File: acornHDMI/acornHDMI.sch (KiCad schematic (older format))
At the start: 33 parts, among them J1 0.1\" grid male, J2 8P8C_Shielded, J3 HDMI_A, U1 PTN3381D, U2 PCA9534

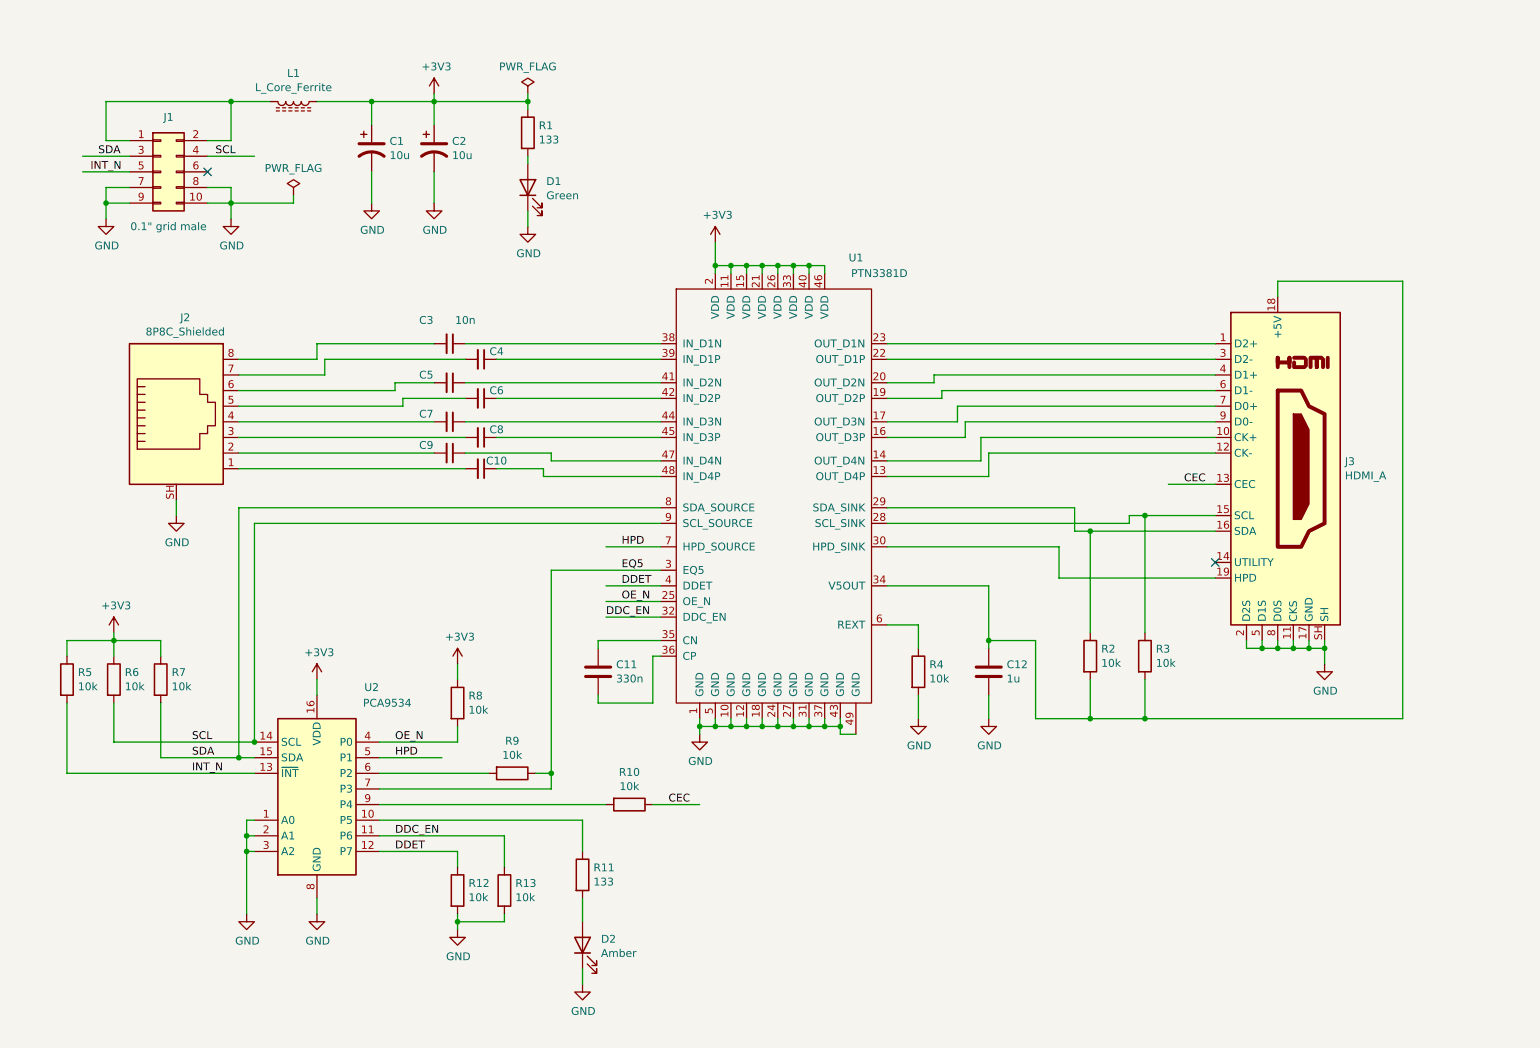
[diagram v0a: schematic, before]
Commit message: change PTN3381D to B
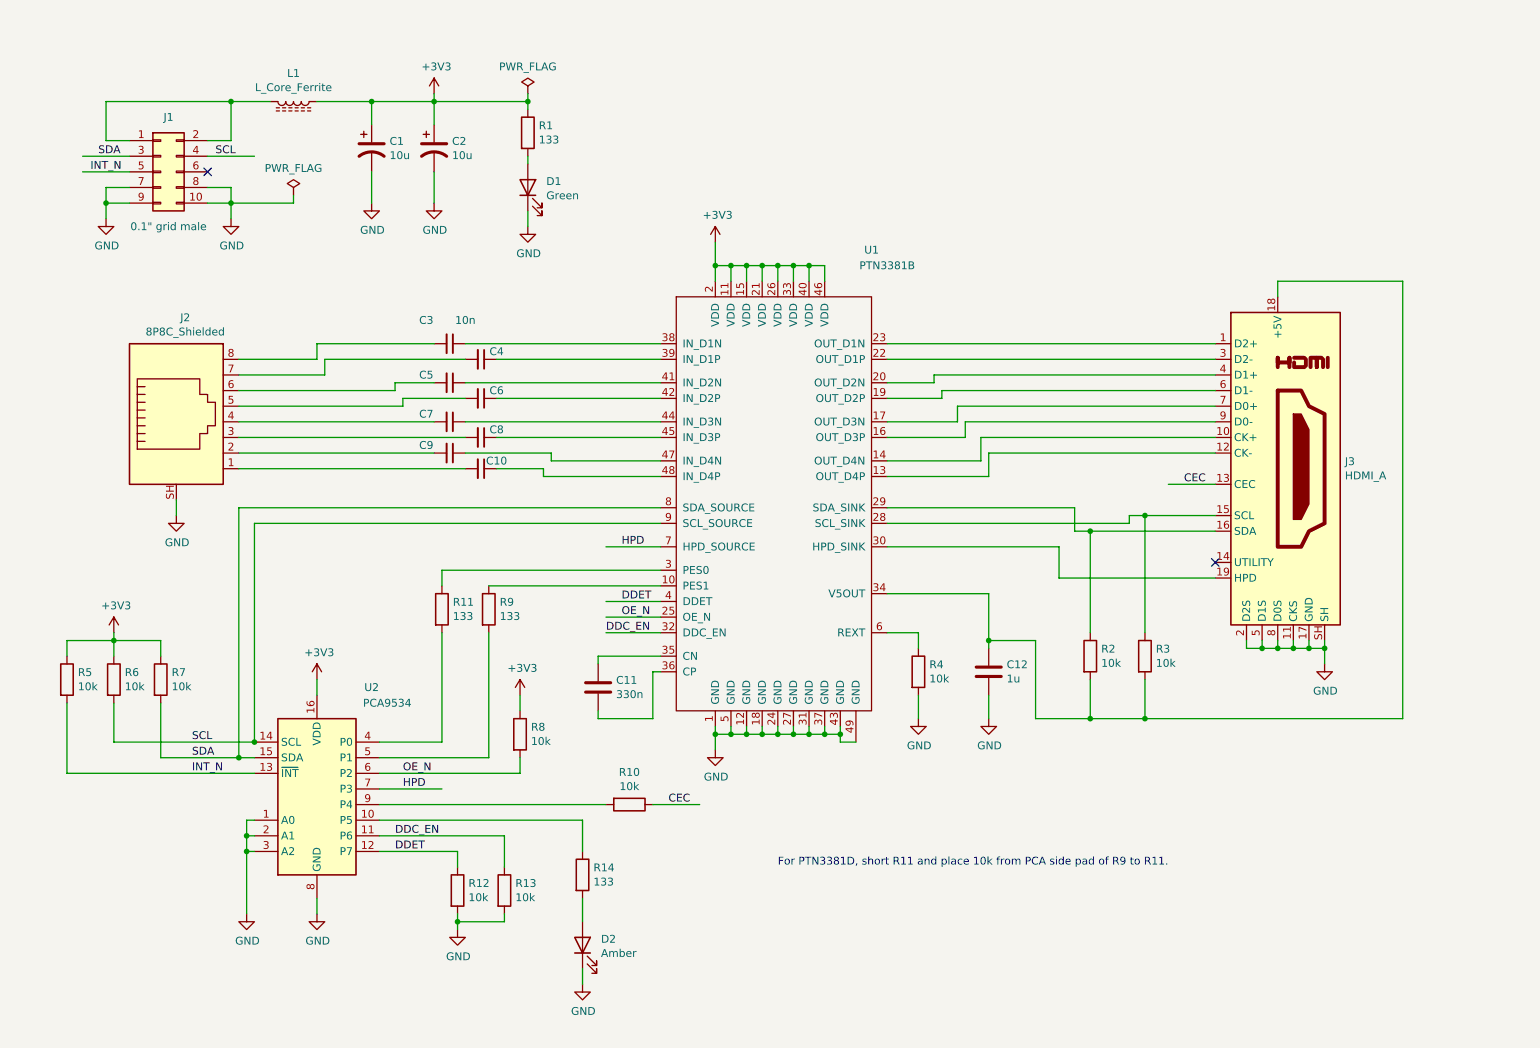
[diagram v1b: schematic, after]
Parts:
- removed U1: PTN3381D, Package_DFN_QFN:QFN-48-1EP_7x7mm_P0.5mm_EP5.15x5.15mm, symbol local:PTN3381D
- added R14: 133, Resistor_SMD:R_0603_1608Metric_Pad0.98x0.95mm_HandSolder, symbol Device:R
- added U1: PTN3381B, Package_DFN_QFN:QFN-48-1EP_7x7mm_P0.5mm_EP5.15x5.15mm, symbol local:PTN3381B
- R9: value 10k -> 133
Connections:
- net labels removed: EQ5
- wire segments 220 -> 219
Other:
- note added: "For PTN3381D, short R11 and place 10k from PCA side pad of R9 to R11."
- moved on the sheet: C11, R11, R8
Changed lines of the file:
@@
 $EndDescr
-$Comp
-L local:PTN3381D U1
-U 1 1 60D4AADB
-P 5400 5200
-F 0 "U1" H 5950 8050 50  0000 C CNN
-F 1 "PTN3381D" H 6100 7950 50  0000 C CNN
-F 2 "Package_DFN_QFN:QFN-48-1EP_7x7mm_P0.5mm_EP5.15x5.15mm" H 5400 5250 50  0001 C CNN
-F 3 "" H 5400 5250 50  0001 C CNN
-	1    5400 5200
-	1    0    0    -1
-$EndComp
 $Comp
 L Connector:HDMI_A J3
@@
 $EndComp
 Wire Wire Line
-	6150 4700 6350 4700
-Wire Wire Line
 	6350 5150 6350 5300
 $Comp
@@
 L power:GND #PWR0102
 U 1 1 60D5A843
-P 4950 5400
-F 0 "#PWR0102" H 4950 5150 50  0001 C CNN
-F 1 "GND" H 4955 5227 50  0000 C CNN
-F 2 "" H 4950 5400 50  0001 C CNN
-F 3 "" H 4950 5400 50  0001 C CNN
-	1    4950 5400
-	1    0    0    -1
-$EndComp
-Wire Wire Line
-	4950 5400 4950 5350
-Wire Wire Line
-	4950 5350 5050 5350
-Wire Wire Line
-	5050 5350 5050 5300
-Connection ~ 4950 5350
-Wire Wire Line
-	4950 5350 4950 5300
-Wire Wire Line
-	5150 5300 5150 5350
-Wire Wire Line
-	5150 5350 5050 5350
-Connection ~ 5050 5350
-Wire Wire Line
-	5250 5300 5250 5350
-Wire Wire Line
-	5250 5350 5150 5350
-Connection ~ 5150 5350
-Wire Wire Line
-	5350 5300 5350 5350
-Wire Wire Line
-	5350 5350 5250 5350
-Connection ~ 5250 5350
-Wire Wire Line
-	5950 5400 5850 5400
-Wire Wire Line
-	5850 5400 5850 5350
-Wire Wire Line
-	5850 5350 5750 5350
-Connection ~ 5350 5350
-Wire Wire Line
-	5850 5300 5850 5350
-Connection ~ 5850 5350
-Wire Wire Line
-	5750 5300 5750 5350
-Connection ~ 5750 5350
-Wire Wire Line
-	5750 5350 5650 5350
-Wire Wire Line
-	5650 5300 5650 5350
-Connection ~ 5650 5350
-Wire Wire Line
-	5650 5350 5550 5350
-Wire Wire Line
-	5550 5300 5550 5350
-Connection ~ 5550 5350
-Wire Wire Line
-	5550 5350 5450 5350
-Wire Wire Line
-	5450 5300 5450 5350
-Connection ~ 5450 5350
-Wire Wire Line
-	5450 5350 5350 5350
+P 5050 5500
+F 0 "#PWR0102" H 5050 5250 50  0001 C CNN
+F 1 "GND" H 5055 5327 50  0000 C CNN
+F 2 "" H 5050 5500 50  0001 C CNN
+F 3 "" H 5050 5500 50  0001 C CNN
+	1    5050 5500
+	1    0    0    -1
+$EndComp
+Wire Wire Line
+	5050 5400 5050 5350
+Wire Wire Line
+	5150 5350 5150 5400
+Wire Wire Line
+	5150 5400 5050 5400
+Wire Wire Line
+	5250 5350 5250 5400
+Wire Wire Line
+	5250 5400 5150 5400
+Connection ~ 5150 5400
+Wire Wire Line
+	5350 5350 5350 5400
+Wire Wire Line
+	5350 5400 5250 5400
+Connection ~ 5250 5400
+Wire Wire Line
+	5950 5450 5850 5450
+Wire Wire Line
+	5850 5450 5850 5400
+Wire Wire Line
+	5850 5400 5750 5400
+Connection ~ 5350 5400
+Wire Wire Line
+	5850 5350 5850 5400
+Connection ~ 5850 5400
+Wire Wire Line
+	5750 5350 5750 5400
+Connection ~ 5750 5400
+Wire Wire Line
+	5750 5400 5650 5400
+Wire Wire Line
+	5650 5350 5650 5400
+Connection ~ 5650 5400
+Wire Wire Line
+	5650 5400 5550 5400
+Wire Wire Line
+	5550 5350 5550 5400
+Connection ~ 5550 5400
+Wire Wire Line
+	5550 5400 5450 5400
+Wire Wire Line
+	5450 5350 5450 5400
+Connection ~ 5450 5400
+Wire Wire Line
+	5450 5400 5350 5400
 Wire Wire Line
 	6150 2900 8250 2900
@@
 	8850 4850 8950 4850
 Wire Wire Line
-	6150 4450 6800 4450
-Wire Wire Line
 	9450 5300 9450 2500
 Wire Wire Line
@@
 $EndComp
 Wire Wire Line
-	6350 4850 6350 4700
+	6350 4850 6350 4750
 Wire Wire Line
 	7250 4200 7250 4400
@@
 Connection ~ 6800 4800
 Wire Wire Line
-	6800 4800 6800 4450
+	6800 4800 6800 4500
 Wire Wire Line
 	7100 5300 7450 5300
@@
 L Device:C C11
 U 1 1 60DBDA44
-P 4300 5000
-F 0 "C11" H 4415 5046 50  0000 L CNN
-F 1 "330n" H 4415 4955 50  0000 L CNN
-F 2 "Capacitor_SMD:C_0603_1608Metric_Pad1.08x0.95mm_HandSolder" H 4338 4850 50  0001 C CNN
-F 3 "~" H 4300 5000 50  0001 C CNN
-	1    4300 5000
+P 4300 5100
+F 0 "C11" H 4415 5146 50  0000 L CNN
+F 1 "330n" H 4415 5055 50  0000 L CNN
+F 2 "Capacitor_SMD:C_0603_1608Metric_Pad1.08x0.95mm_HandSolder" H 4338 4950 50  0001 C CNN
+F 3 "~" H 4300 5100 50  0001 C CNN
+	1    4300 5100
 	1    0    0    -1
 $EndComp
@@
 	3650 3000 4700 3000
 Wire Wire Line
-	4700 4800 4300 4800
-Wire Wire Line
-	4300 4800 4300 4850
-Wire Wire Line
-	4300 5150 4300 5200
-Wire Wire Line
-	4300 5200 4650 5200
-Wire Wire Line
-	4650 5200 4650 4900
-Wire Wire Line
-	4650 4900 4700 4900
-Text Label 3000 5450 0    50   ~ 0
+	4700 4900 4300 4900
+Wire Wire Line
+	4300 4900 4300 4950
+Wire Wire Line
+	4300 5250 4300 5300
+Wire Wire Line
+	4300 5300 4650 5300
+Text Label 3050 5650 0    50   ~ 0
 OE_N
 Wire Wire Line
+	4350 4650 4700 4650
+Text Label 4450 4650 0    50   ~ 0
+OE_N
+Wire Wire Line
 	4350 4550 4700 4550
+Wire Wire Line
+	4350 4750 4700 4750
 Text Label 4450 4550 0    50   ~ 0
-OE_N
-Wire Wire Line
-	4350 4450 4700 4450
-Wire Wire Line
-	4350 4650 4700 4650
-Text Label 4450 4450 0    50   ~ 0
 DDET
 Text Label 3000 6150 0    50   ~ 0
@@
 L Device:R R8
 U 1 1 60E82787
-P 3400 5200
-F 0 "R8" H 3470 5246 50  0000 L CNN
-F 1 "10k" H 3470 5155 50  0000 L CNN
-F 2 "Resistor_SMD:R_0603_1608Metric_Pad0.98x0.95mm_HandSolder" V 3330 5200 50  0001 C CNN
-F 3 "~" H 3400 5200 50  0001 C CNN
-	1    3400 5200
-	1    0    0    -1
-$EndComp
-Wire Wire Line
-	3400 5450 3400 5350
-Wire Wire Line
-	2900 5450 3400 5450
-Text Label 4350 4650 0    50   ~ 0
+P 3800 5400
+F 0 "R8" H 3870 5446 50  0000 L CNN
+F 1 "10k" H 3870 5355 50  0000 L CNN
+F 2 "Resistor_SMD:R_0603_1608Metric_Pad0.98x0.95mm_HandSolder" V 3730 5400 50  0001 C CNN
+F 3 "~" H 3800 5400 50  0001 C CNN
+	1    3800 5400
+	1    0    0    -1
+$EndComp
+Wire Wire Line
+	3800 5650 3800 5550
+Text Label 4350 4750 0    50   ~ 0
 DDC_EN
-Text Label 4450 4350 0    50   ~ 0
-EQ5
 $Comp
 L Device:R R12
@@
 	3650 3700 3950 3700
 Wire Wire Line
-	2900 5550 3300 5550
-Text Label 3000 5550 0    50   ~ 0
+	2900 5750 3300 5750
+Text Label 3050 5750 0    50   ~ 0
 HPD
 $Comp
@@
 Text Label 8050 3800 0    50   ~ 0
 CEC
-$Comp
-L Device:R R9
-U 1 1 60EF1912
-P 3750 5650
-F 0 "R9" V 3543 5650 50  0000 C CNN
-F 1 "10k" V 3634 5650 50  0000 C CNN
-F 2 "Resistor_SMD:R_0603_1608Metric_Pad0.98x0.95mm_HandSolder" V 3680 5650 50  0001 C CNN
-F 3 "~" H 3750 5650 50  0001 C CNN
-	1    3750 5650
-	0    1    1    0
-$EndComp
 Wire Wire Line
 	2900 5850 4350 5850
-Wire Wire Line
-	2900 5650 3600 5650
-Wire Wire Line
-	2900 5750 4000 5750
-Wire Wire Line
-	4000 5750 4000 5650
-Wire Wire Line
-	4000 5650 3900 5650
-Wire Wire Line
-	4000 5650 4000 4350
-Wire Wire Line
-	4000 4350 4700 4350
-Connection ~ 4000 5650
 $Comp
 L Device:LED D2
@@
 L Device:R R11
 U 1 1 60DB9809
-P 4200 6300
-F 0 "R11" H 4270 6346 50  0000 L CNN
-F 1 "133" H 4270 6255 50  0000 L CNN
-F 2 "Resistor_SMD:R_0603_1608Metric_Pad0.98x0.95mm_HandSolder" V 4130 6300 50  0001 C CNN
-F 3 "~" H 4200 6300 50  0001 C CNN
-	1    4200 6300
+P 3300 4600
+F 0 "R11" H 3370 4646 50  0000 L CNN
+F 1 "133" H 3370 4555 50  0000 L CNN
+F 2 "Resistor_SMD:R_0603_1608Metric_Pad0.98x0.95mm_HandSolder" V 3230 4600 50  0001 C CNN
+F 3 "~" H 3300 4600 50  0001 C CNN
+	1    3300 4600
 	1    0    0    -1
 $EndComp
@@
 $EndComp
 Wire Wire Line
-	5050 2450 5050 2400
-Wire Wire Line
-	5750 2450 5750 2400
-Wire Wire Line
 	5750 2400 5650 2400
 Connection ~ 5050 2400
 Wire Wire Line
 	5050 2400 5050 2250
-Wire Wire Line
-	5150 2450 5150 2400
 Connection ~ 5150 2400
 Wire Wire Line
 	5150 2400 5050 2400
-Wire Wire Line
-	5250 2450 5250 2400
 Connection ~ 5250 2400
 Wire Wire Line
 	5250 2400 5150 2400
-Wire Wire Line
-	5350 2450 5350 2400
 Connection ~ 5350 2400
 Wire Wire Line
 	5350 2400 5250 2400
-Wire Wire Line
-	5450 2450 5450 2400
 Connection ~ 5450 2400
 Wire Wire Line
 	5450 2400 5350 2400
-Wire Wire Line
-	5550 2450 5550 2400
 Connection ~ 5550 2400
 Wire Wire Line
 	5550 2400 5450 2400
-Wire Wire Line
-	5650 2450 5650 2400
 Connection ~ 5650 2400
 Wire Wire Line
@@
 L power:+3V3 #PWR0119
 U 1 1 60EEE2D6
-P 3400 4950
-F 0 "#PWR0119" H 3400 4800 50  0001 C CNN
-F 1 "+3V3" H 3415 5123 50  0000 C CNN
-F 2 "" H 3400 4950 50  0001 C CNN
-F 3 "" H 3400 4950 50  0001 C CNN
-	1    3400 4950
-	1    0    0    -1
-$EndComp
-Wire Wire Line
-	3400 5050 3400 4950
+P 3800 5150
+F 0 "#PWR0119" H 3800 5000 50  0001 C CNN
+F 1 "+3V3" H 3815 5323 50  0000 C CNN
+F 2 "" H 3800 5150 50  0001 C CNN
+F 3 "" H 3800 5150 50  0001 C CNN
+	1    3800 5150
+	1    0    0    -1
+$EndComp
+Wire Wire Line
+	3800 5250 3800 5150
+$Comp
+L local:PTN3381B U1
+U 1 1 60E8A423
+P 5400 5250
+F 0 "U1" H 6050 8200 50  0000 C CNN
+F 1 "PTN3381B" H 6150 8100 50  0000 C CNN
+F 2 "Package_DFN_QFN:QFN-48-1EP_7x7mm_P0.5mm_EP5.15x5.15mm" H 5400 5300 50  0001 C CNN
+F 3 "" H 5400 5300 50  0001 C CNN
+	1    5400 5250
+	1    0    0    -1
+$EndComp
+Wire Wire Line
+	6150 4500 6800 4500
+Wire Wire Line
+	6150 4750 6350 4750
+Wire Wire Line
+	4650 5300 4650 5000
+Wire Wire Line
+	4650 5000 4700 5000
+Wire Wire Line
+	5050 5400 5050 5500
+Connection ~ 5050 5400
+Wire Wire Line
+	2900 5650 3800 5650
+$Comp
+L Device:R R9
+U 1 1 60F836D5
+P 3600 4600
+F 0 "R9" H 3670 4646 50  0000 L CNN
+F 1 "133" H 3670 4555 50  0000 L CNN
+F 2 "Resistor_SMD:R_0603_1608Metric_Pad0.98x0.95mm_HandSolder" V 3530 4600 50  0001 C CNN
+F 3 "~" H 3600 4600 50  0001 C CNN
+	1    3600 4600
+	1    0    0    -1
+$EndComp
+Wire Wire Line
+	2900 5450 3300 5450
+Wire Wire Line
+	3300 5450 3300 4750
+Wire Wire Line
+	3300 4450 3300 4350
+Wire Wire Line
+	3300 4350 4700 4350
+Wire Wire Line
+	2900 5550 3600 5550
+Wire Wire Line
+	3600 5550 3600 4750
+Wire Wire Line
+	3600 4450 4700 4450
+$Comp
+L Device:R R14
+U 1 1 60FBBD51
+P 4200 6300
+F 0 "R14" H 4270 6346 50  0000 L CNN
+F 1 "133" H 4270 6255 50  0000 L CNN
+F 2 "Resistor_SMD:R_0603_1608Metric_Pad0.98x0.95mm_HandSolder" V 4130 6300 50  0001 C CNN
+F 3 "~" H 4200 6300 50  0001 C CNN
+	1    4200 6300
+	1    0    0    -1
+$EndComp
+Wire Wire Line
+	5050 2400 5050 2500
+Wire Wire Line
+	5150 2400 5150 2500
+Wire Wire Line
+	5250 2400 5250 2500
+Wire Wire Line
+	5350 2400 5350 2500
+Wire Wire Line
+	5450 2400 5450 2500
+Wire Wire Line
+	5550 2400 5550 2500
+Wire Wire Line
+	5650 2400 5650 2500
+Wire Wire Line
+	5750 2400 5750 2500
+Text Notes 5450 6250 0    50   ~ 0
+For PTN3381D, short R11 and place 10k from PCA side pad of R9 to R11.
 $EndSCHEMATC

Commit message: change to 3M 7700 cable
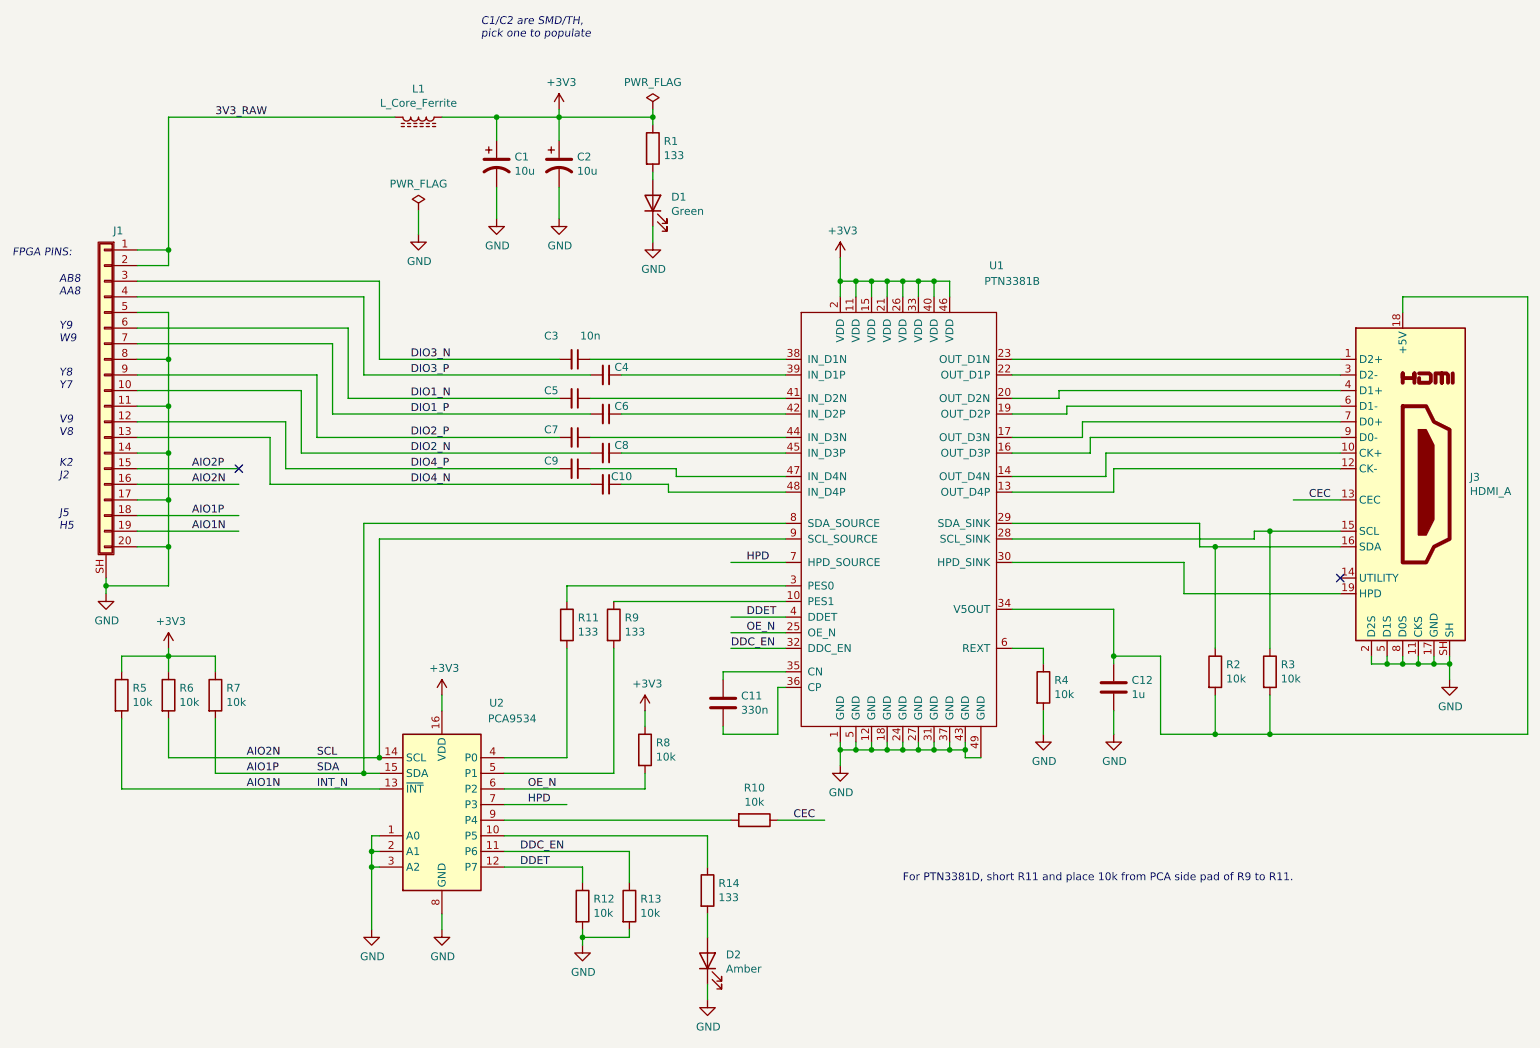
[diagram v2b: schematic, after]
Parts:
- removed J1: 0.1\" grid male, Connector_IDC:IDC-Header_2x05_P2.54mm_Vertical, symbol Connector_Generic:Conn_02x05_Odd_Even
- removed J2: 8P8C_Shielded, local:RJCSE-x380-01, symbol Connector:8P8C_Shielded
- added J1: Conn_01x20_Shielded, local:3M_7700_20, symbol Connector_Generic_Shielded:Conn_01x20_Shielded
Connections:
- net labels added: 3V3_RAW, AIO1N, AIO1P, AIO2N, AIO2P, DIO1_N, DIO1_P, DIO2_N, DIO2_P, DIO3_N, DIO3_P, DIO4_N, DIO4_P
- wire segments 219 -> 232
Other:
- note added: "AB8\nAA8"
- note added: "C1/C2 are SMD/TH,\npick one to populate"
- note added: "FPGA PINS:"
- note added: "K2\nJ2\n\n\nJ5\nH5"
- note added: "V9\nV8"
- note added: "Y8\nY7"
- note added: "Y9\nW9"
- moved on the sheet: C1, C10, C11, C12, C2, C3, C4, C5, C6, C7, C8, C9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

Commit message: routing in progress
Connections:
- net labels added: H_5V, H_CK+, H_CK-, H_D0+, H_D0-, H_D1+, H_D1-, H_D2+, H_D2-, H_HPD, H_SCL, H_SDA
- net labels removed: AIO1N, AIO1P, AIO2N
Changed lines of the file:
@@
 Text Label 1700 3700 0    50   ~ 0
 AIO2P
-Text Label 1700 3800 0    50   ~ 0
-AIO2N
-Text Label 1700 4000 0    50   ~ 0
-AIO1P
-Text Label 1700 4100 0    50   ~ 0
-AIO1N
 Text Notes 850  4100 0    50   Italic 0
 K2\nJ2\n\n\nJ5\nH5
@@
 Wire Wire Line
 	1250 5750 2900 5750
-Text Label 2050 5550 0    50   ~ 0
-AIO2N
-Text Label 2050 5650 0    50   ~ 0
-AIO1P
-Text Label 2050 5750 0    50   ~ 0
-AIO1N
 Text Notes 3550 950  0    50   Italic 0
 C1/C2 are SMD/TH,\npick one to populate
+Text Label 8700 4500 0    50   ~ 0
+H_HPD
+Text Label 9000 5400 0    50   ~ 0
+H_5V
+Text Label 7550 4050 0    50   ~ 0
+H_SDA
+Text Label 7550 4150 0    50   ~ 0
+H_SCL
+Text Label 8100 3000 0    50   ~ 0
+H_D2+
+Text Label 8100 3100 0    50   ~ 0
+H_D2-
+Text Label 8200 3200 0    50   ~ 0
+H_D1+
+Text Label 8200 3300 0    50   ~ 0
+H_D1-
+Text Label 8300 3400 0    50   ~ 0
+H_D0+
+Text Label 8300 3500 0    50   ~ 0
+H_D0-
+Text Label 8400 3600 0    50   ~ 0
+H_CK+
+Text Label 8400 3700 0    50   ~ 0
+H_CK-
+Text Label 1750 3800 0    50   ~ 0
+SCL
+Text Label 1750 4000 0    50   ~ 0
+SDA
+Text Label 1700 4100 0    50   ~ 0
+INT_N
 $EndSCHEMATC
